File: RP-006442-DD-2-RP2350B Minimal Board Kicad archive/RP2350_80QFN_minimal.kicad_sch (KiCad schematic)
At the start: 50 parts, among them J1 USB_C_Receptacle_USB2.0_16P, J2 Conn_02x26_Odd_Even, J3 Conn_02x26_Odd_Even, SW1 SW_Push, SW2 SW_Push, U1 RP2350_80QFN, U2 NCP1117-3.3_SOT223, U3 W25Q128JVS, U4 DNF, Y1 ABM8-272-T3

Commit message: Update
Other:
- sheet Input buttons ports: added GPIO22, GPIO23, GPIO24, GPIO25, GPIO26, GPIO27, GPIO28, GPIO29, GPIO30, GPIO31, GPIO32, GPIO33; removed none

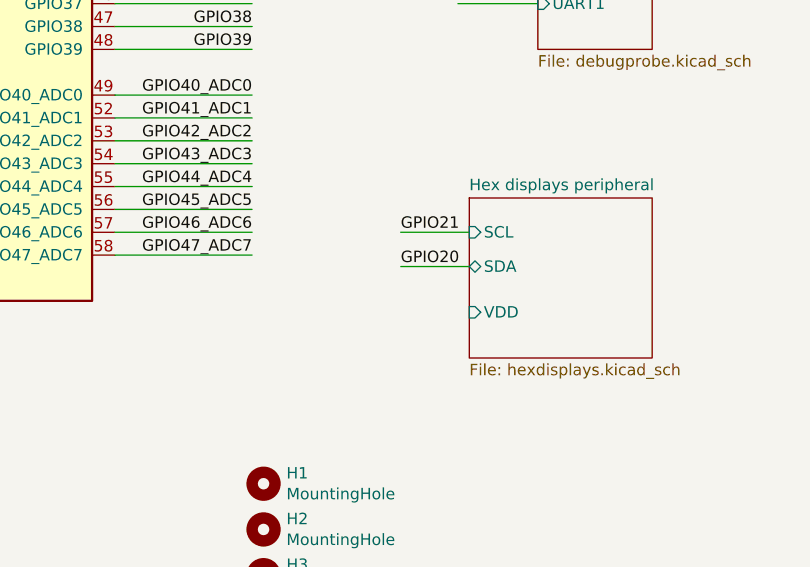
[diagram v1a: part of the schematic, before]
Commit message: VBUS to VDD connection
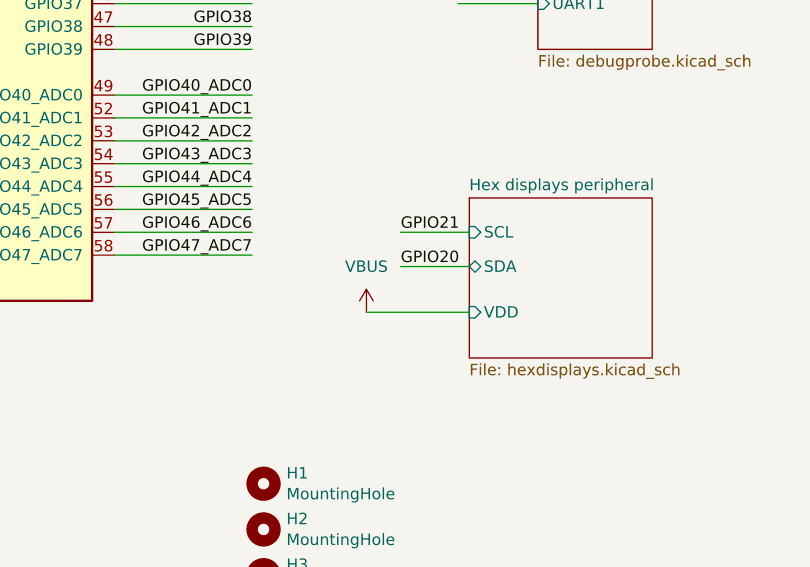
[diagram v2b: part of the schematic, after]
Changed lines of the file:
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@@
 	(wire
 		(pts
+			(xy 262.89 240.03) (xy 274.32 240.03)
+		)
+		(stroke
+			(width 0)
+			(type default)
+		)
+	)
+	(wire
+		(pts
 			(xy 209.55 81.28) (xy 212.09 81.28)
 		)
@@
 					(unit 1)
 				)
+			)
+		)
+	)
+	(symbol
+		(lib_name "VBUS_1")
+		(lib_id "power:VBUS")
+		(at 262.89 240.03 0)
+		(unit 1)
+		(exclude_from_sim no)
+		(in_bom yes)
+		(on_board yes)
+		(dnp no)
+		(fields_autoplaced yes)
+		(property "Reference" "#PWR060"
+			(at 262.89 243.84 0)
+			(effects
+				(font
+					(size 1.27 1.27)
+				)
+				(hide yes)
+			)
+		)
+		(property "Value" "VBUS"
+			(at 262.89 234.95 0)
+			(effects
+				(font
+					(size 1.27 1.27)
+				)
+			)
+		)
+		(property "Footprint" ""
+			(at 262.89 240.03 0)
+			(effects
+				(font
+					(size 1.27 1.27)
+				)
+				(hide yes)
+			)
+		)
+		(property "Datasheet" ""
+			(at 262.89 240.03 0)
+			(effects
+				(font
+					(size 1.27 1.27)
+				)
+				(hide yes)
+			)
+		)
+		(property "Description" "Power symbol creates a global label with name \"VBUS\""
+			(at 262.89 240.03 0)
+			(effects
+				(font
+					(size 1.27 1.27)
+				)
+				(hide yes)
+			)
+		)
+		(pin "1"
+		)
+		(instances
+			(project ""
+				(path "/94683f5c-9cd9-448e-be96-9792537b5cb8"
+					(reference "#PWR060")
+					(unit 1)
+				)

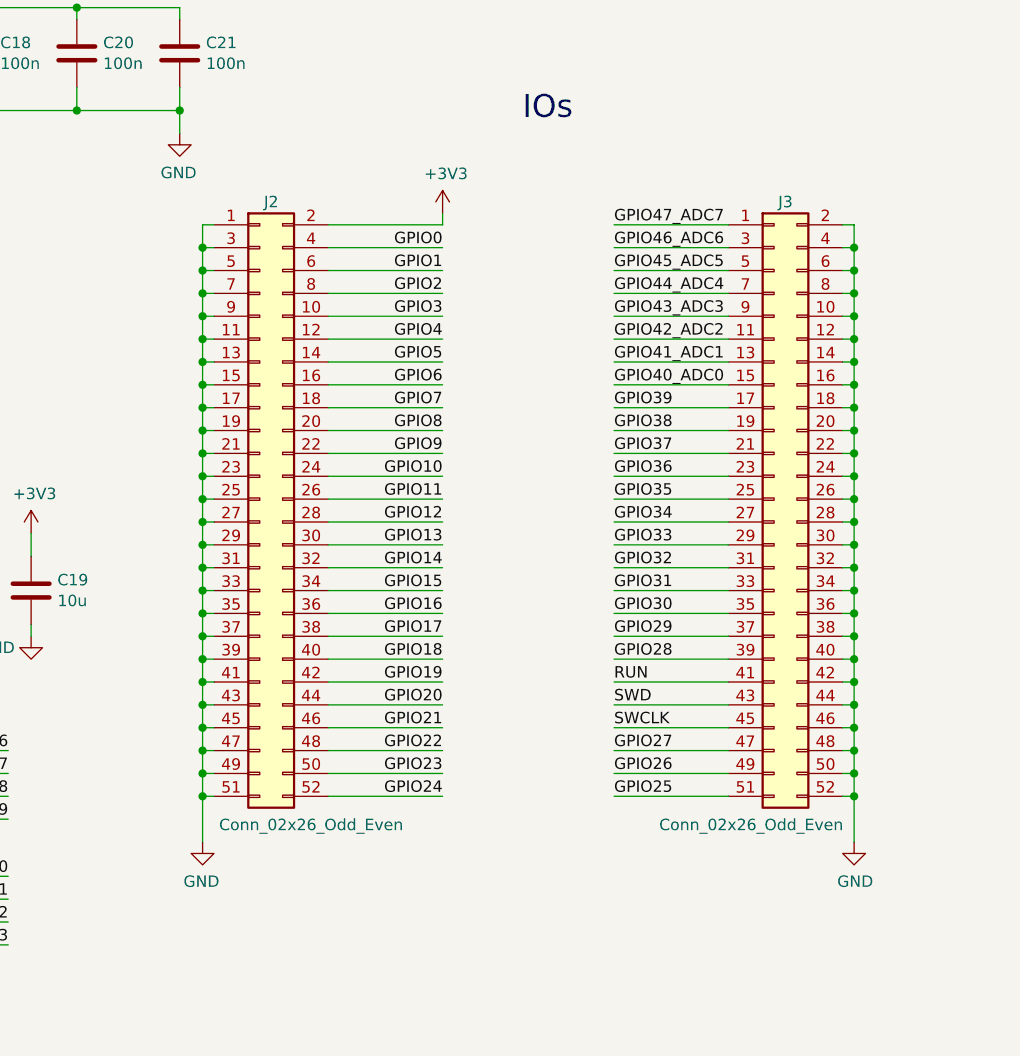
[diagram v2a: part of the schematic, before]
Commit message: Update
fixed some errors in electrical rules checker
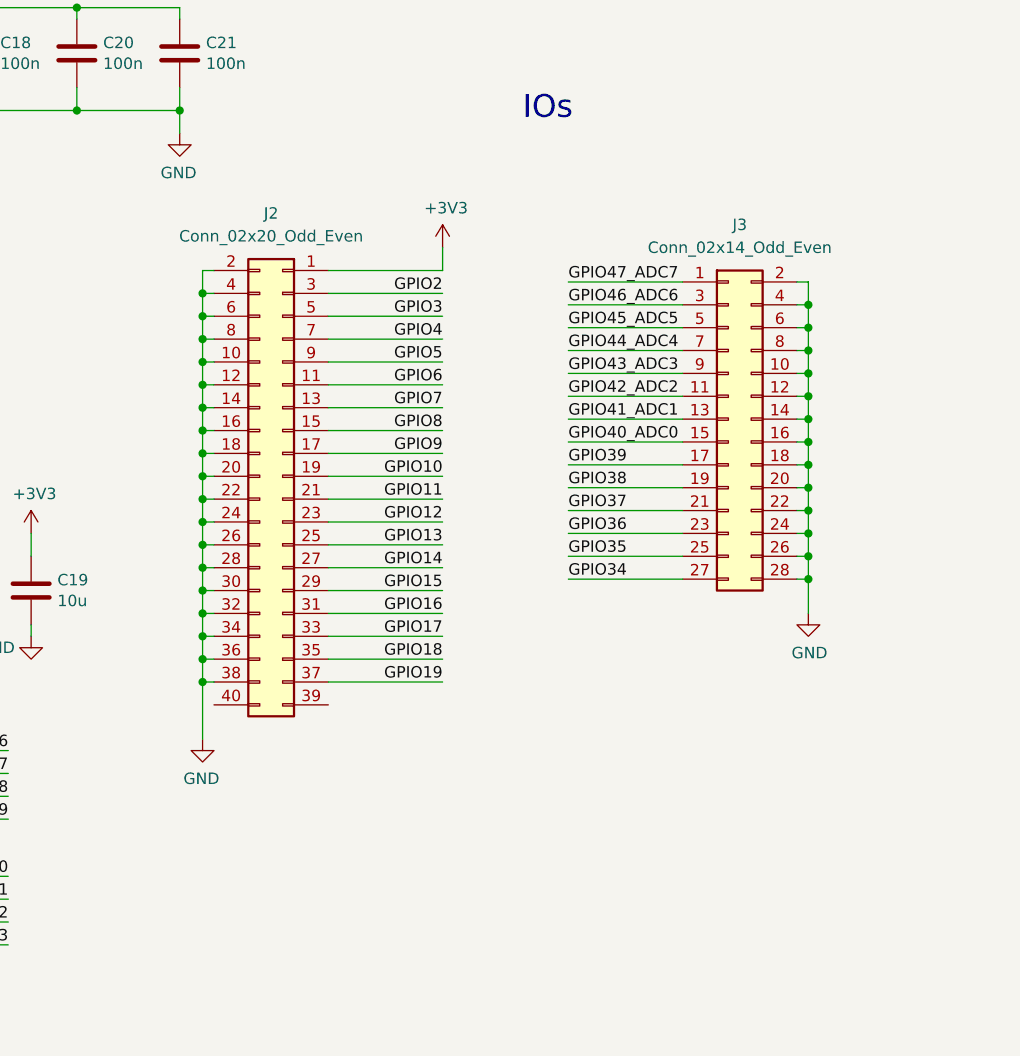
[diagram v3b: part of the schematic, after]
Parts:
- removed J2, J3: Conn_02x26_Odd_Even, Connector_PinHeader_2.54mm:PinHeader_2x26_P2.54mm_Vertical, symbol Connector_Generic:Conn_02x26_Odd_Even
- added J2: Conn_02x20_Odd_Even, Connector_PinSocket_2.54mm:PinSocket_2x20_P2.54mm_Vertical, symbol Connector_Generic:Conn_02x20_Odd_Even
- added J3: Conn_02x14_Odd_Even, Connector_PinSocket_2.54mm:PinSocket_2x14_P2.54mm_Vertical, symbol Connector_Generic:Conn_02x14_Odd_Even
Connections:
- net +3V3: now also J2.1 (Pin_1)
- net GND: now also J2.10 (Pin_10), J2.12 (Pin_12), J2.14 (Pin_14), J2.16 (Pin_16), J2.18 (Pin_18), J2.2 (Pin_2), J2.20 (Pin_20), J2.22 (Pin_22), J2.24 (Pin_24), J2.26 (Pin_26), J2.28 (Pin_28), J2.30 (Pin_30), J2.32 (Pin_32), J2.34 (Pin_34), J2.36 (Pin_36), J2.38 (Pin_38), J2.4 (Pin_4), J2.6 (Pin_6), J2.8 (Pin_8), J3.10 (Pin_10), J3.12 (Pin_12), J3.14 (Pin_14), J3.16 (Pin_16), J3.18 (Pin_18), J3.2 (Pin_2), J3.20 (Pin_20), J3.22 (Pin_22), J3.24 (Pin_24), J3.26 (Pin_26), J3.28 (Pin_28), J3.4 (Pin_4), J3.6 (Pin_6), J3.8 (Pin_8)
- net GPIO10: now also J2.19 (Pin_19)
- net GPIO11: now also J2.21 (Pin_21)
- net GPIO12: now also J2.23 (Pin_23)
- net GPIO13: now also J2.25 (Pin_25)
- net GPIO14: now also J2.27 (Pin_27)
- net GPIO15: now also J2.29 (Pin_29)
- net GPIO16: now also J2.31 (Pin_31)
- net GPIO17: now also J2.33 (Pin_33)
- net GPIO18: now also J2.35 (Pin_35)
- net GPIO19: now also J2.37 (Pin_37)
- net GPIO2: now also J2.3 (Pin_3)
- net GPIO3: now also J2.5 (Pin_5)
- net GPIO34: now also J3.27 (Pin_27)
- net GPIO35: now also J3.25 (Pin_25)
- net GPIO36: now also J3.23 (Pin_23)
- net GPIO37: now also J3.21 (Pin_21)
- net GPIO38: now also J3.19 (Pin_19)
- net GPIO39: now also J3.17 (Pin_17)
- net GPIO4: now also J2.7 (Pin_7)
- net GPIO40_ADC0: now also J3.15 (Pin_15)
- net GPIO41_ADC1: now also J3.13 (Pin_13)
- net GPIO42_ADC2: now also J3.11 (Pin_11)
- net GPIO43_ADC3: now also J3.9 (Pin_9)
- net GPIO44_ADC4: now also J3.7 (Pin_7)
- net GPIO45_ADC5: now also J3.5 (Pin_5)
- net GPIO46_ADC6: now also J3.3 (Pin_3)
- net GPIO47_ADC7: now also J3.1 (Pin_1)
- net GPIO5: now also J2.9 (Pin_9)
- net GPIO6: now also J2.11 (Pin_11)
- net GPIO7: now also J2.13 (Pin_13)
- net GPIO8: now also J2.15 (Pin_15)
- net GPIO9: now also J2.17 (Pin_17)

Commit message: small update
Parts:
- removed J3: Conn_02x14_Odd_Even, Connector_PinSocket_2.54mm:PinSocket_2x14_P2.54mm_Vertical, symbol Connector_Generic:Conn_02x14_Odd_Even
- added J3: Conn_02x09_Odd_Even, Connector_PinHeader_2.54mm:PinHeader_2x09_P2.54mm_Vertical, symbol Connector_Generic:Conn_02x09_Odd_Even
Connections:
- net GND: now also J3.10 (Pin_10), J3.12 (Pin_12), J3.14 (Pin_14), J3.16 (Pin_16), J3.18 (Pin_18), J3.2 (Pin_2), J3.4 (Pin_4), J3.6 (Pin_6), J3.8 (Pin_8)
- net GPIO39: now also J3.17 (Pin_17)
- net GPIO40_ADC0: now also J3.15 (Pin_15)
- net GPIO41_ADC1: now also J3.13 (Pin_13)
- net GPIO42_ADC2: now also J3.11 (Pin_11)
- net GPIO43_ADC3: now also J3.9 (Pin_9)
- net GPIO44_ADC4: now also J3.7 (Pin_7)
- net GPIO45_ADC5: now also J3.5 (Pin_5)
- net GPIO46_ADC6: now also J3.3 (Pin_3)
- net GPIO47_ADC7: now also J3.1 (Pin_1)
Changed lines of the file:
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@@
-	)
-	(symbol
-		(lib_id "Connector_Generic:Conn_02x14_Odd_Even")
-		(at 381 106.68 0)
-		(unit 1)
-		(exclude_from_sim no)
-		(in_bom yes)
-		(on_board yes)
-		(dnp no)
-		(fields_autoplaced yes)
-		(property "Reference" "J3"
-			(at 382.27 85.09 0)
-			(effects
-				(font
-					(size 1.27 1.27)
-				)
-			)
-		)
-		(property "Value" "Conn_02x14_Odd_Even"
-			(at 382.27 87.63 0)
-			(effects
-				(font
-					(size 1.27 1.27)
-				)
-			)
-		)
-		(property "Footprint" "Connector_PinSocket_2.54mm:PinSocket_2x14_P2.54mm_Vertical"
-			(at 381 106.68 0)
-			(effects
-				(font
-					(size 1.27 1.27)
-				)
-				(hide yes)
-			)
-		)
-		(property "Datasheet" "~"
-			(at 381 106.68 0)
-			(effects
-				(font
-					(size 1.27 1.27)
-				)
-				(hide yes)
-			)
-		)
-		(property "Description" "Generic connector, double row, 02x14, odd/even pin numbering scheme (row 1 odd numbers, row 2 even numbers), script generated (kicad-library-utils/schlib/autogen/connector/)"
-			(at 381 106.68 0)
-			(effects
-				(font
-					(size 1.27 1.27)
-				)
-				(hide yes)
-			)
-		)
-		(pin "3"
-		)
-		(pin "5"
-		)
-		(pin "7"
-		)
-		(pin "9"
-		)
-		(pin "11"
-		)
-		(pin "13"
-		)
-		(pin "15"
-		)
-		(pin "17"
-		)
-		(pin "19"
-		)
-		(pin "21"
-		)
-		(pin "23"
-		)
-		(pin "25"
-		)
-		(pin "27"
-		)
-		(pin "2"
-		)
-		(pin "4"
-		)
-		(pin "6"
-		)
-		(pin "8"
-		)
-		(pin "10"
-		)
-		(pin "12"
-		)
-		(pin "14"
-		)
-		(pin "16"
-		)
-		(pin "18"
-		)
-		(pin "20"
-		)
-		(pin "22"
-		)
-		(pin "24"
-		)
-		(pin "26"
-		)
-		(pin "28"
-		)
-		(pin "1"
-		)
-		(instances
-			(project ""
-				(path "/94683f5c-9cd9-448e-be96-9792537b5cb8"
-					(reference "J3")
-					(unit 1)
-				)
-			)
-		)
 	)
 	(symbol
@@
 					(unit 1)
 				)
+			)
+		)
+	)
+	(symbol
+		(lib_id "Connector_Generic:Conn_02x09_Odd_Even")
+		(at 381 101.6 0)
+		(unit 1)
+		(exclude_from_sim no)
+		(in_bom yes)
+		(on_board yes)
+		(dnp no)
+		(fields_autoplaced yes)
+		(property "Reference" "J3"
+			(at 382.27 85.09 0)
+			(effects
+				(font
+					(size 1.27 1.27)
+				)
+			)
+		)
+		(property "Value" "Conn_02x09_Odd_Even"
+			(at 382.27 87.63 0)
+			(effects
+				(font
+					(size 1.27 1.27)
+				)
+			)
+		)
+		(property "Footprint" "Connector_PinHeader_2.54mm:PinHeader_2x09_P2.54mm_Vertical"
+			(at 381 101.6 0)
+			(effects
+				(font
+					(size 1.27 1.27)
+				)
+				(hide yes)
+			)
+		)
+		(property "Datasheet" "~"
+			(at 381 101.6 0)
+			(effects
+				(font
+					(size 1.27 1.27)
+				)
+				(hide yes)
+			)
+		)
+		(property "Description" "Generic connector, double row, 02x09, odd/even pin numbering scheme (row 1 odd numbers, row 2 even numbers), script generated (kicad-library-utils/schlib/autogen/connector/)"
+			(at 381 101.6 0)
+			(effects
+				(font
+					(size 1.27 1.27)
+				)
+				(hide yes)
+			)
+		)
+		(pin "1"
+		)
+		(pin "3"
+		)
+		(pin "5"
+		)
+		(pin "7"
+		)
+		(pin "9"
+		)
+		(pin "11"
+		)
+		(pin "13"
+		)
+		(pin "15"
+		)
+		(pin "17"
+		)
+		(pin "2"
+		)
+		(pin "4"
+		)
+		(pin "6"
+		)
+		(pin "8"
+		)
+		(pin "10"
+		)
+		(pin "12"
+		)
+		(pin "14"
+		)
+		(pin "16"
+		)
+		(pin "18"
+		)
+		(instances
+			(project ""
+				(path "/94683f5c-9cd9-448e-be96-9792537b5cb8"
+					(reference "J3")
+					(unit 1)
+				)

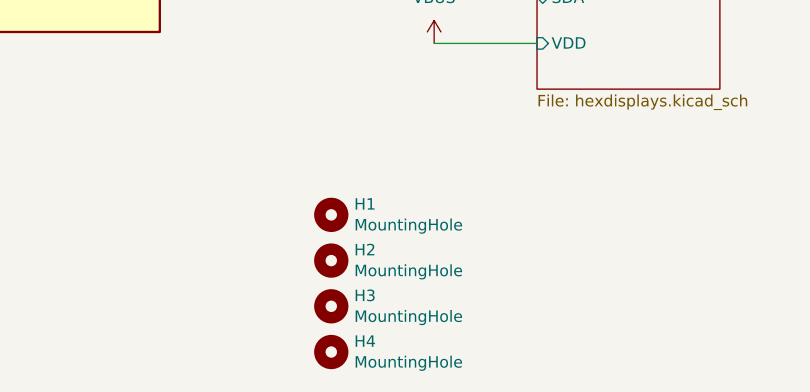
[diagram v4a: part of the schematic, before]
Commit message: Remove mounting holes
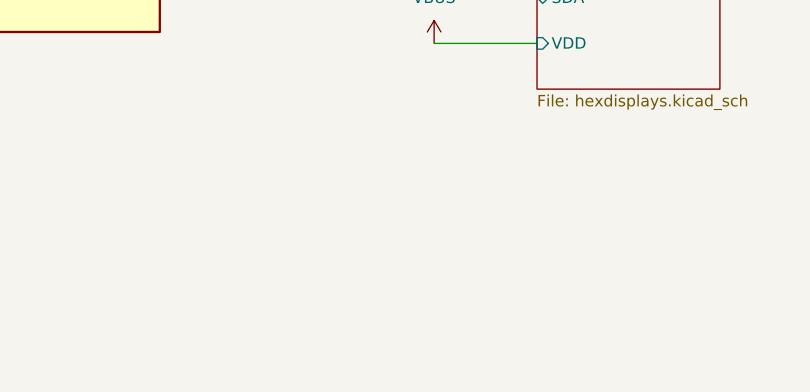
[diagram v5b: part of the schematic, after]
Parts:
- removed H1, H2, H3, H4: MountingHole, MountingHole:MountingHole_2.7mm_M2.5, symbol Mechanical:MountingHole

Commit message: Update RP2350_80QFN_minimal.kicad_sch
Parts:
- removed J2: Conn_02x20_Odd_Even, Connector_PinSocket_2.54mm:PinSocket_2x20_P2.54mm_Vertical, symbol Connector_Generic:Conn_02x20_Odd_Even
- added J2: Conn_02x19_Odd_Even, Connector_PinSocket_2.54mm:PinSocket_2x19_P2.54mm_Vertical, symbol Connector_Generic:Conn_02x19_Odd_Even
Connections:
- net +3V3: now also J2.1 (Pin_1)
- net GND: now also J2.10 (Pin_10), J2.12 (Pin_12), J2.14 (Pin_14), J2.16 (Pin_16), J2.18 (Pin_18), J2.2 (Pin_2), J2.20 (Pin_20), J2.22 (Pin_22), J2.24 (Pin_24), J2.26 (Pin_26), J2.28 (Pin_28), J2.30 (Pin_30), J2.32 (Pin_32), J2.34 (Pin_34), J2.36 (Pin_36), J2.38 (Pin_38), J2.4 (Pin_4), J2.6 (Pin_6), J2.8 (Pin_8)
- net GPIO10: now also J2.19 (Pin_19)
- net GPIO11: now also J2.21 (Pin_21)
- net GPIO12: now also J2.23 (Pin_23)
- net GPIO13: now also J2.25 (Pin_25)
- net GPIO14: now also J2.27 (Pin_27)
- net GPIO15: now also J2.29 (Pin_29)
- net GPIO16: now also J2.31 (Pin_31)
- net GPIO17: now also J2.33 (Pin_33)
- net GPIO18: now also J2.35 (Pin_35)
- net GPIO19: now also J2.37 (Pin_37)
- net GPIO2: now also J2.3 (Pin_3)
- net GPIO3: now also J2.5 (Pin_5)
- net GPIO4: now also J2.7 (Pin_7)
- net GPIO5: now also J2.9 (Pin_9)
- net GPIO6: now also J2.11 (Pin_11)
- net GPIO7: now also J2.13 (Pin_13)
- net GPIO8: now also J2.15 (Pin_15)
- net GPIO9: now also J2.17 (Pin_17)
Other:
- company: Raspberry Pi Ltd -> (none)
- title: RP2350B QFN80 Minimal Design Example -> Lab Platform Prototype Thesis Project
